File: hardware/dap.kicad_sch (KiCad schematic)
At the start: 0 parts

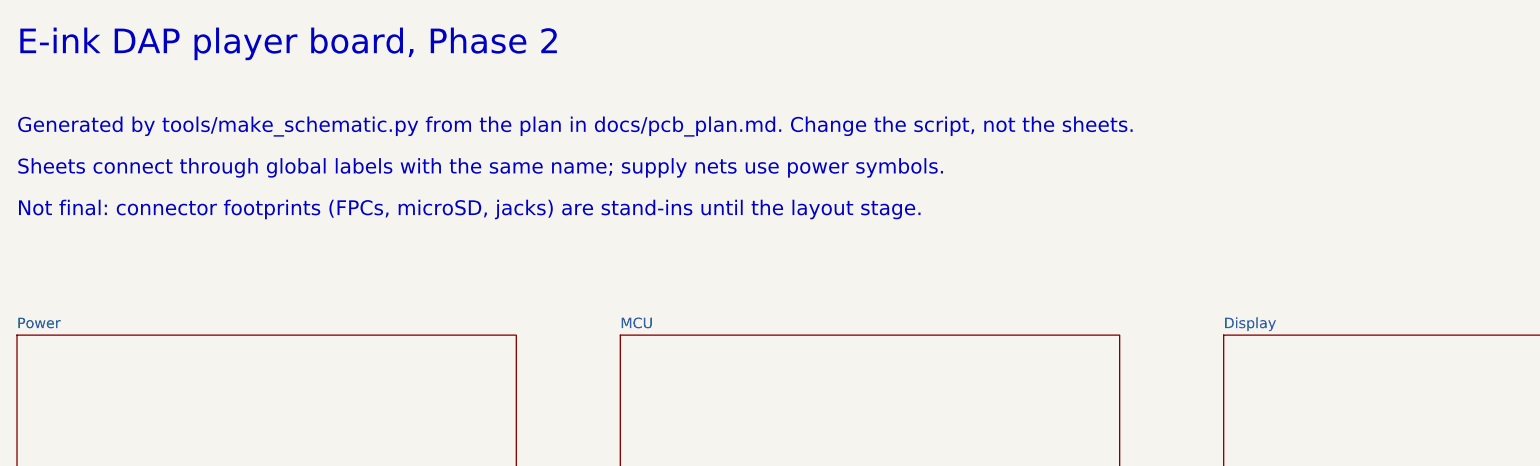
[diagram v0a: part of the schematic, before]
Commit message: Use the chosen parts in the schematic, with their LCSC numbers
The headphone jacks are now real parts. The 3.5 mm SHOU HAN PJ-342 is a
3-pole stereo jack, per its drawing: tip 3, ring 6, sleeve 5 and 2, and a
switch on tip and ring that touches them while no plug is in. Its tip
switch drives the left DAC's HP_DETECT, so the firmware sets
HPDETECT_INV. The 4.4 mm jack is the Kinghelm KH-PJ-44002-12DBAP-A: two
pins per pole in Pentaconn order and a separate plug switch from DET_44
to ground.

Checked against the datasheets: the oscillators' OE is high or open =
running and tri-state when low, so they can share MCLK; the GL823K's VDD
and VDDA are both its own 3.3 V. The CS43131 FILT capacitors are 22 uF
0805 25 V now, about 15-19 uF under bias where a 15 uF part would keep
about 11. The e-paper circuit follows the GDEY037T03-T02 reference: VPP
(pin 19) left open and a 1 MOhm gate pull-down, R1 and R2 in 0603.

Every assembled part has an LCSC number: the passives are in a table
checked on lcsc.com. 49.9k had no stock, so the TPS2553 limit resistor is
47k (about 0.5 A). The touch and microSD footprints are the real ones.
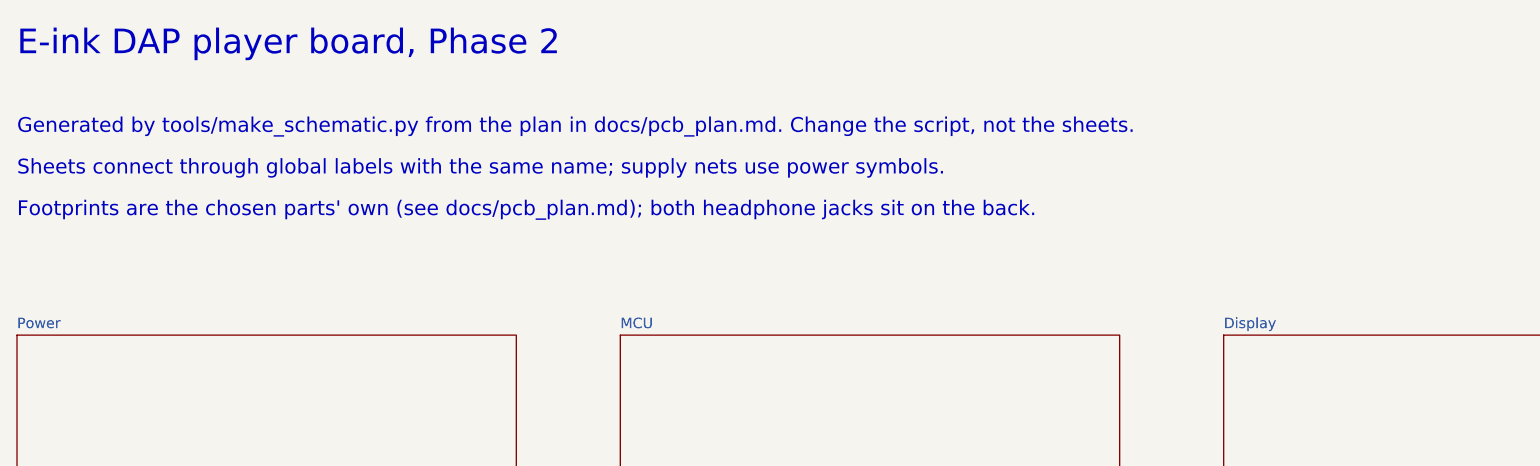
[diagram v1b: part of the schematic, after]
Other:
- note added: "Footprints are the chosen parts' own (see docs/pcb_plan.md); both headphone jacks sit on the back."
- note removed: "Not final: connector footprints (FPCs, microSD, jacks) are stand-ins until the layout stage."
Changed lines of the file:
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@@
 		(instances
 			(project "dap"
-				(path "/60ec8d80-1a0f-4f3f-be0e-afd5ea83a336"
+				(path "/5378fb4e-51c2-49a9-8be7-a02ccfde9411"
 					(page "2")
 				)
@@
 		(instances
 			(project "dap"
-				(path "/60ec8d80-1a0f-4f3f-be0e-afd5ea83a336"
+				(path "/5378fb4e-51c2-49a9-8be7-a02ccfde9411"
 					(page "3")
 				)
@@
 		(instances
 			(project "dap"
-				(path "/60ec8d80-1a0f-4f3f-be0e-afd5ea83a336"
+				(path "/5378fb4e-51c2-49a9-8be7-a02ccfde9411"
 					(page "4")
 				)
@@
 		(instances
 			(project "dap"
-				(path "/60ec8d80-1a0f-4f3f-be0e-afd5ea83a336"
+				(path "/5378fb4e-51c2-49a9-8be7-a02ccfde9411"
 					(page "5")
 				)
@@
 		(instances
 			(project "dap"
-				(path "/60ec8d80-1a0f-4f3f-be0e-afd5ea83a336"
+				(path "/5378fb4e-51c2-49a9-8be7-a02ccfde9411"
 					(page "6")
 				)
@@
 		)
 	)
-	(text "Not final: connector footprints (FPCs, microSD, jacks) are stand-ins until the layout stage."
+	(text "Footprints are the chosen parts' own (see docs/pcb_plan.md); both headphone jacks sit on the back."
 		(exclude_from_sim no)
 		(at 25.4 45.72 0)
